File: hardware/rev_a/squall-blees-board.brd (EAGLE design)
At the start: 48.3 x 50.2 mm, 7 parts, among them J1 SQUALL_HEADER, J4 HIROSE-DF40C-10DP-0.4V, J5 HIROSE-DF40C-10DP-0.4V

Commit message: Work on circuit board
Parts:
- removed J2, J3: (no value), pinhead:2X08
- removed J6: (no value), pinhead:1X01
- added C1: 10uF, passives:0603_CAP
- added C2, C3, C4: 100nF, passives:0402_CAP
- added U$1: TSL2560DFN, blees:DFN2
- added U1: HTU21DDFN, blees:DFN
- added U2: LPS331APQFN, blees:HCLGA-16L
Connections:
- net 5V: no longer J6.1
- net A5: no longer J3.5, J3.6
- net A6: no longer J3.3, J3.4
- net A7: no longer J3.1, J3.2
- net GND: now also C1.2, C2.2, C3.2, C4.2, U$1.2, U$1.3, U1.2, U1.PAD, U2.10, U2.12, U2.13, U2.16, U2.5, U2.7; no longer J2.15, J2.16
- net MISO: no longer J3.10, J3.9
- net MOSI: no longer J3.7, J3.8
- net P22: no longer J2.3, J2.4
- net P23: no longer J2.5, J2.6
- net P24: no longer J2.7, J2.8
- net P25: no longer J2.10, J2.9
- net SCL: now also U$1.4, U1.6, U2.4; no longer J2.13, J2.14
- net SCLK: no longer J3.11, J3.12
- net SDA: now also U$1.6, U1.1, U2.6; no longer J2.11, J2.12
- net SWDCLK: no longer J3.13, J3.14
- net SWDIO/!RESET: no longer J3.15, J3.16
- net VCC: now also C1.1, C2.1, C3.1, C4.1, U$1.1, U1.5, U2.1, U2.14, U2.15, U2.8; no longer J2.1, J2.2
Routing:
- net P25: track 24.1 -> 9.90 mm
- net SDA: track 34.8 -> 20.6 mm
- net SCL: track 36.3 -> 22.1 mm
- net P24: track 21.5 -> 9.34 mm
- net A6: track 25.7 -> 14.5 mm
- net A7: track 27.1 -> 16.0 mm
- net A5: track 21.0 -> 9.85 mm
- net GND: track 53.9 -> 45.3 mm
- net VCC: track 18.2 -> 12.1 mm
- net P23: track 21.4 -> 17.4 mm
- net P22: track 20.3 -> 16.2 mm
- net MOSI: track 14.1 -> 9.99 mm
- net MISO: track 16.1 -> 12.0 mm
- net SCLK: track 13.9 -> 9.84 mm
- net SWDIO/!RESET: track 20.5 -> 17.5 mm
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
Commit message: Board finished
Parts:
- removed LOGO1: UMICH_SOLID_TINY, logos:UMICH_SOLID_50MIL
- removed U$1: TSL2560DFN, blees:DFN2
- removed U1: HTU21DDFN, blees:DFN
- removed U2: LPS331APQFN, blees:HCLGA-16L
- added LIGHT: TSL2560DFN, blees:DFN2
- added PRESSURE: LPS331APQFN, blees:HCLGA-16L
- added R1, R2: 2kΩ, passives:0402_RES
- added TEMP/HUMID: HTU21DDFN, blees:DFN
- moved C3 12.9 mm to (13.5, 8.38), turned to 90 degrees
- moved C2 4.83 mm to (19.8, 19.1), turned to 270 degrees
- moved C4 4.54 mm to (29.5, 18.8), turned to 270 degrees
- moved C1 4.52 mm to (17.3, 18.8), turned to 270 degrees
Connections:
- net GND: now also LIGHT.2, LIGHT.3, PRESSURE.10, PRESSURE.12, PRESSURE.13, PRESSURE.16, PRESSURE.5, PRESSURE.7, TEMP/HUMID.2, TEMP/HUMID.PAD; no longer U$1.2, U$1.3, U1.2, U1.PAD, U2.10, U2.12, U2.13, U2.16, U2.5, U2.7
- net SCL: now also LIGHT.4, PRESSURE.4, R2.1, TEMP/HUMID.6; no longer U$1.4, U1.6, U2.4
- net SDA: now also LIGHT.6, PRESSURE.6, R1.1, TEMP/HUMID.1; no longer U$1.6, U1.1, U2.6
- net VCC: now also LIGHT.1, PRESSURE.1, PRESSURE.14, PRESSURE.15, PRESSURE.8, R1.2, R2.2, TEMP/HUMID.5; no longer U$1.1, U1.5, U2.1, U2.14, U2.15, U2.8
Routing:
- net VCC: track 12.1 -> 58.9 mm
- net SCL: track 22.1 -> 40.1 mm, vias 1 -> 2
- net SDA: track 20.6 -> 37.7 mm, vias 1 -> 4
- net P22: track 16.2 -> 2.54 mm
- net SWDIO/!RESET: track 17.5 -> 4.61 mm, vias 2 -> 1
- net P23: track 17.4 -> 4.48 mm
- net SWDCLK: track 16.7 -> 5.32 mm, vias 2 -> 1
- net A7: track 16.0 -> 5.20 mm
- net A6: track 14.5 -> 5.71 mm
- net MISO: track 12.0 -> 4.34 mm
- net GND: track 45.3 -> 37.9 mm, vias 7 -> 6
- net SCLK: track 9.84 -> 2.54 mm
- net A5: track 9.85 -> 3.05 mm
- net MOSI: track 9.99 -> 3.86 mm
- net P25: track 9.90 -> 4.69 mm
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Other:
- board size 48.3 x 50.2 mm -> 48.3 x 50.1 mm
- board text added: "BLEES"
- board text added: "EECS 373"
- board text removed: "3V3"
- board text removed: "5V"
- board text removed: "A"
- board text removed: "A5"
- board text removed: "A6"
- board text removed: "A7"
- board text removed: "Brad Campbell"
- board text removed: "GND"
- board text removed: "MISO"
- board text removed: "MOSI"
- board text removed: "P22"
- board text removed: "P23"
- board text removed: "P24"
- board text removed: "P25"
- board text removed: "SCL"
- board text removed: "SCLK"
- board text removed: "SDA"
- board text removed: "SWDC"
- board text removed: "SWDI"
- board text removed: "Squall Breakout"
- board text removed: "VCC"

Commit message: Board ready for prod
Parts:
- moved LIGHT 4.71 mm to (28.1, 17.6)
- moved R2 4.15 mm to (32.0, 16.3)
- moved C4 3.82 mm to (25.7, 18.1)
- moved R1 3.40 mm to (33.2, 16.3)
- moved C3 2.98 mm to (16.1, 6.91), turned to 270 degrees
- moved PRESSURE 2.77 mm to (21.5, 17.2)
- moved C2 2.75 mm to (17.1, 18.9)
- moved TEMP/HUMID 2.42 mm to (18.6, 7.37)
- moved C1 1.15 mm to (18.4, 18.8)
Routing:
- net MOSI: track 3.86 -> 9.50 mm
- net 5V: track 5.65 -> 10.6 mm
- net VCC: track 58.9 -> 63.8 mm, vias 1 -> 2
- net SDA: track 37.7 -> 42.0 mm, vias 4 -> 5
- net SCL: track 40.1 -> 36.6 mm, vias 2 -> 1
- net GND: track 37.9 -> 41.4 mm, vias 6 -> 12
- net MISO: track 4.34 -> 7.75 mm
- net SCLK: track 2.54 -> 5.40 mm
- net SWDIO/!RESET: track 4.61 -> 7.37 mm
- net SWDCLK: track 5.32 -> 4.11 mm
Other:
- board size 48.3 x 50.1 mm -> 25.4 x 21 mm
- board text added: "Caleb Pratt"
- board text added: "DATE"
- board text added: "Nate Jones"
- board text added: "Nick Bertoldi"
- board text added: "Scott Su"
- board text added: "V1.0"

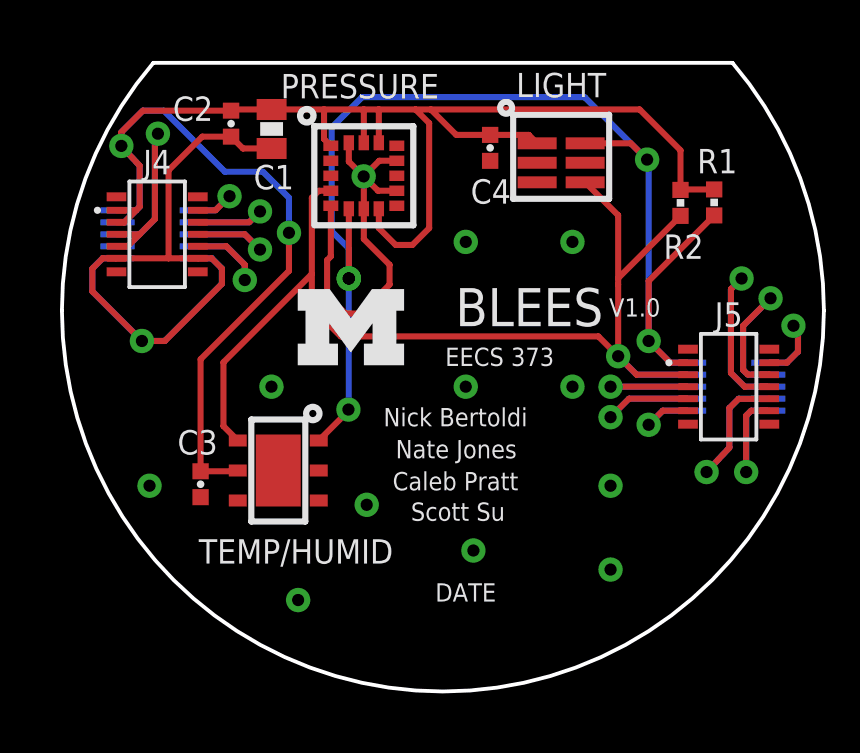
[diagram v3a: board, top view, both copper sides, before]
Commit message: Make changes to text, output gerbers, panelize
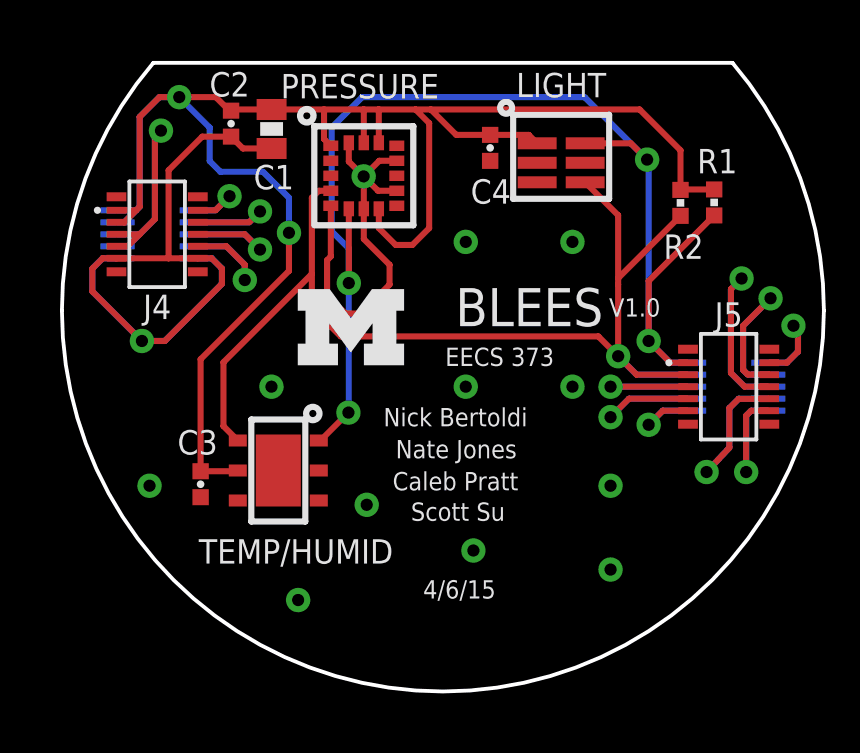
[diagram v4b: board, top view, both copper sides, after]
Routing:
- net SDA: track 42.0 -> 42.2 mm, vias 5 -> 4
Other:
- board text added: "4/6/15"
- board text removed: "DATE"
